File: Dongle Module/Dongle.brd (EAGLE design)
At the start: 45 x 28 mm, 29 parts, among them Q2 2.5A/30V, U1 RFM69HCW, U10 74AHC1G125, U8 ATSAMD21G-A, U9 3.3V, Y1 32.768kHz

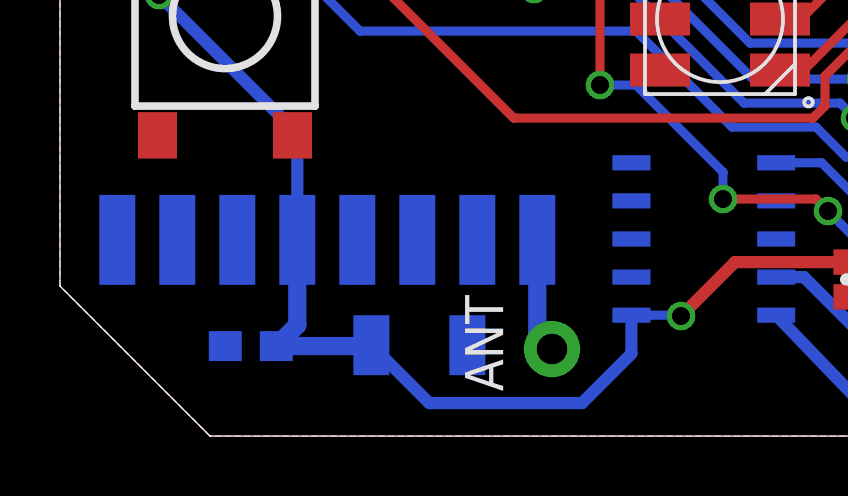
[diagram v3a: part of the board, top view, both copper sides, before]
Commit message: Added the interrupt line from the RFM69 into the Camera Module board. It is connected to GPIO_24
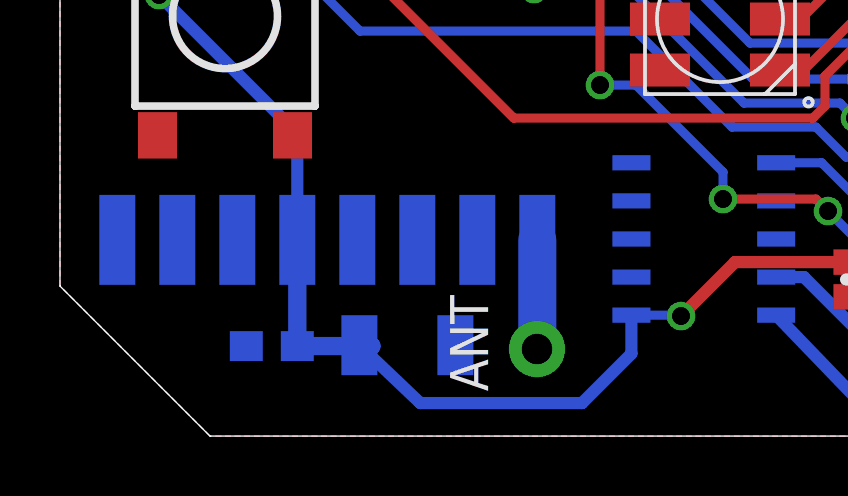
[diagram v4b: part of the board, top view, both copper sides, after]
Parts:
- moved C2 0.70 mm to (7.06, 3.00)
- moved ANT 0.50 mm to (15.9, 2.90)
- moved C1 0.40 mm to (11.6, 3.03)
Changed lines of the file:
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@@
 </autorouter>
 <elements>
-<element name="C1" library="SparkFun-Capacitors" package="1210" value="10uF" x="11.98" y="3.03" smashed="yes" rot="MR180">
-<attribute name="PROD_ID" value="CAP-09824" x="11.98" y="3.03" size="1.778" layer="28" rot="MR180" display="off"/>
-<attribute name="NAME" x="12.32" y="2.77" size="0.4064" layer="26" rot="MR0"/>
+<element name="C1" library="SparkFun-Capacitors" package="1210" value="10uF" x="11.58" y="3.03" smashed="yes" rot="MR180">
+<attribute name="PROD_ID" value="CAP-09824" x="11.58" y="3.03" size="1.778" layer="28" rot="MR180" display="off"/>
+<attribute name="NAME" x="11.92" y="2.77" size="0.4064" layer="26" rot="MR0"/>
 </element>
 <element name="C12" library="SparkFun-Capacitors" package="0402-CAP" value="0.1uF" x="34.25" y="15.33" smashed="yes">
@@
 <attribute name="NAME" x="26.628" y="17.711" size="0.4064" layer="25" font="vector" rot="R90"/>
 </element>
-<element name="C2" library="SparkFun-Capacitors" package="0603-CAP@1" value="0.1uF" x="6.36" y="3" smashed="yes" rot="MR0">
-<attribute name="PROD_ID" value="CAP-00810" x="6.36" y="3" size="1.778" layer="28" rot="MR0" display="off"/>
-<attribute name="NAME" x="6.649" y="4.162" size="0.4064" layer="26" font="vector" rot="MR0"/>
+<element name="C2" library="SparkFun-Capacitors" package="0603-CAP@1" value="0.1uF" x="7.06" y="3" smashed="yes" rot="MR0">
+<attribute name="PROD_ID" value="CAP-00810" x="7.06" y="3" size="1.778" layer="28" rot="MR0" display="off"/>
+<attribute name="NAME" x="7.349" y="4.162" size="0.4064" layer="26" font="vector" rot="MR0"/>
 </element>
 <element name="D7" library="SparkFun-LED" package="LED-0603" value="RED" x="43.34" y="21.8" smashed="yes" rot="R180">
@@
 <attribute name="VALUE" x="25.3" y="18" size="1.27" layer="27" font="vector" rot="R180"/>
 </element>
-<element name="ANT" library="SparkFun-Connectors" package="1X01_NO_SILK" value="" x="16.4" y="2.9" smashed="yes">
-<attribute name="NAME" x="14.7712" y="1.4938" size="1.27" layer="25" rot="R90"/>
-<attribute name="VALUE" x="15.13" y="-0.275" size="1.27" layer="27"/>
+<element name="ANT" library="SparkFun-Connectors" package="1X01_NO_SILK" value="" x="15.9" y="2.9" smashed="yes">
+<attribute name="NAME" x="14.2712" y="1.4938" size="1.27" layer="25" rot="R90"/>
+<attribute name="VALUE" x="14.63" y="-0.275" size="1.27" layer="27"/>
 </element>
 </elements>
@@
 <wire x1="33.64" y1="15.3" x2="33.42" y2="15.08" width="0.3048" layer="1"/>
 <wire x1="33.42" y1="15.08" x2="33.42" y2="13" width="0.3048" layer="1"/>
-<wire x1="7.91" y1="6.54" x2="7.91" y2="3.7" width="0.6096" layer="16"/>
-<wire x1="7.91" y1="3.7" x2="7.21" y2="3" width="0.6096" layer="16"/>
+<wire x1="7.91" y1="6.54" x2="7.91" y2="3" width="0.6096" layer="16"/>
 <wire x1="27.79" y1="17.55" x2="27.82" y2="17.52" width="0.6096" layer="1"/>
 <wire x1="27.82" y1="17.52" x2="30.0799" y2="17.52" width="0.6096" layer="1"/>
@@
 <wire x1="32.5" y1="4.6" x2="28.4" y2="4.6" width="0.3048" layer="16"/>
 <wire x1="33.42" y1="4.5" x2="33.42" y2="7.48" width="0.3048" layer="1"/>
-<wire x1="10.38" y1="3.03" x2="10.38" y2="3" width="0.6096" layer="16"/>
-<wire x1="10.38" y1="3" x2="7.21" y2="3" width="0.6096" layer="16"/>
+<wire x1="9.98" y1="3.03" x2="10.38" y2="3" width="0.6096" layer="16"/>
+<wire x1="10.38" y1="3" x2="7.91" y2="3" width="0.6096" layer="16"/>
 <via x="20.7" y="4" extent="1-16" drill="0.6"/>
 <wire x1="20.7" y1="4" x2="20.7" y2="4.03" width="0.3048" layer="16"/>
@@
 <wire x1="19.047" y1="4.03" x2="19.047" y2="2.747" width="0.4064" layer="16"/>
 <wire x1="19.047" y1="2.747" x2="17.4" y2="1.1" width="0.4064" layer="16"/>
-<wire x1="17.4" y1="1.1" x2="12.31" y2="1.1" width="0.4064" layer="16"/>
-<wire x1="12.31" y1="1.1" x2="10.38" y2="3.03" width="0.4064" layer="16"/>
+<wire x1="17.4" y1="1.1" x2="12.01" y2="1.1" width="0.4064" layer="16"/>
+<wire x1="12.01" y1="1.1" x2="9.98" y2="3.03" width="0.4064" layer="16"/>
 <wire x1="26.23" y1="5.8" x2="22.5" y2="5.8" width="0.4064" layer="1"/>
 <wire x1="22.5" y1="5.8" x2="20.7" y2="4" width="0.4064" layer="1"/>
@@
 <contactref element="U1" pad="9"/>
 <contactref element="ANT" pad="1"/>
-<wire x1="16.4" y1="2.9" x2="15.91" y2="3.39" width="0.6096" layer="16"/>
-<wire x1="15.91" y1="3.39" x2="15.91" y2="6.54" width="0.6096" layer="16"/>
+<wire x1="15.91" y1="6.54" x2="15.91" y2="3.39" width="1.27" layer="16"/>
+<wire x1="15.91" y1="3.39" x2="15.9" y2="2.9" width="1.27" layer="16" curve="90"/>
 </signal>
 <signal name="V_USB">

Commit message: Updated the RFM69 library to be closer to C. millis() is the only function hat needs to be updated now.
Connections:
- new net RF_INT: U1.14, U8.4
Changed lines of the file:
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@@
 <wire x1="24.7" y1="13.9" x2="24" y2="13.9" width="0.3048" layer="1"/>
+</signal>
+<signal name="RF_INT">
+<contactref element="U1" pad="14"/>
+<contactref element="U8" pad="4"/>
+<wire x1="5.91" y1="6.54" x2="36.92" y2="7.5" width="0" layer="19" extent="1-16"/>
 </signal>
 </signals>

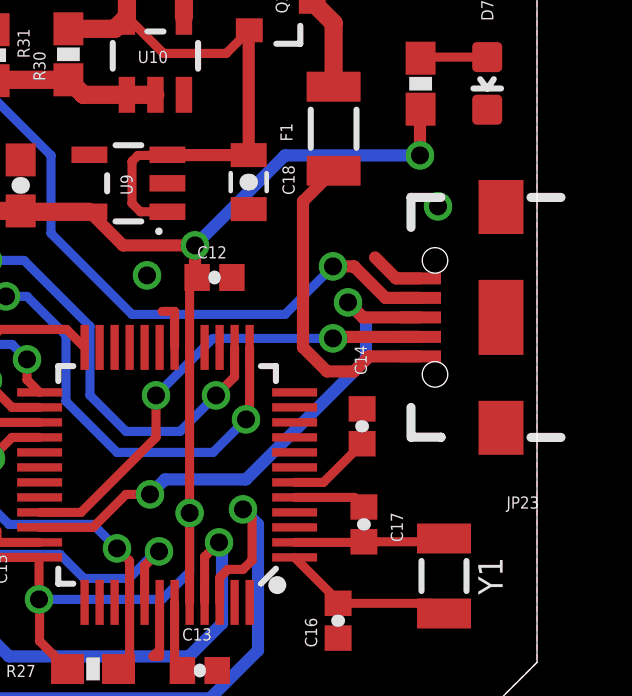
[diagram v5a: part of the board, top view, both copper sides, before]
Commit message: Started the routing of the laser module board Updated the Dongle Module C project to allow for absolute mouse control
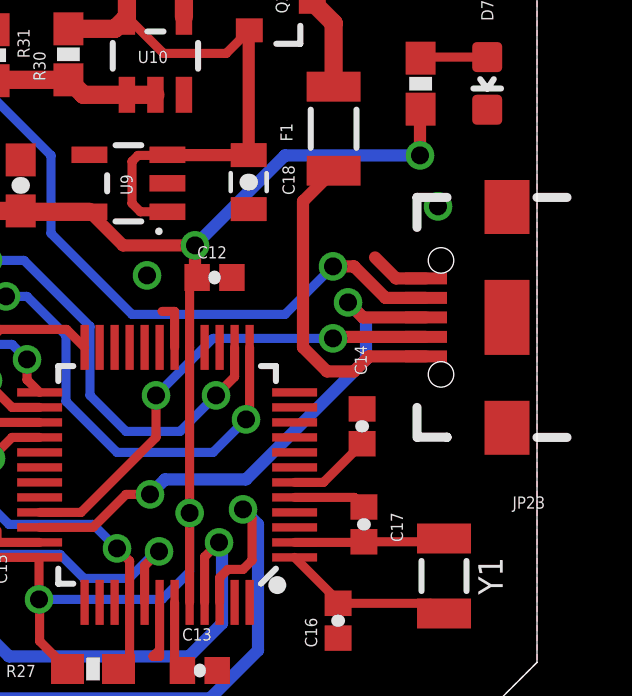
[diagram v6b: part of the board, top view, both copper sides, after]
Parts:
- moved JP23 0.20 mm to (44.0, 14.0)
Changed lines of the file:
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@@
 </element>
 <element name="JP22" library="SparkFun-Connectors" package="SAMTECH_FTSH-105-01" value="CORTEX_DEBUGSMD" x="21.46" y="6.57" smashed="yes" rot="MR90"/>
-<element name="JP23" library="SparkFun-Connectors" package="USB-AB-MICRO-SMD_V03" value="" x="43.8" y="14" rot="R180">
-<attribute name="PROD_ID" value="CONN-11794" x="43.8" y="14" size="1.778" layer="27" rot="R180" display="off"/>
+<element name="JP23" library="SparkFun-Connectors" package="USB-AB-MICRO-SMD_V03" value="" x="44" y="14" rot="R180">
+<attribute name="PROD_ID" value="CONN-11794" x="44" y="14" size="1.778" layer="27" rot="R180" display="off"/>
 </element>
 <element name="Q2" library="SparkFun-DiscreteSemi" package="SOT23-3" value="2.5A/30V" x="36.41" y="24.52" smashed="yes" rot="R270">
@@
 <via x="25.7" y="20.1" extent="1-16" drill="0.6" shape="square"/>
 <via x="41.7" y="17.7" extent="1-16" drill="0.6" shape="square"/>
-<wire x1="41.1" y1="15.3" x2="40.3" y2="15.3" width="0.4064" layer="1"/>
+<wire x1="41.3" y1="15.3" x2="40.3" y2="15.3" width="0.4064" layer="1"/>
 <wire x1="40.3" y1="15.3" x2="39.6" y2="16" width="0.4064" layer="1"/>
 <via x="32" y="15.4" extent="1-16" drill="0.6" shape="square"/>
@@
 <wire x1="38" y1="12.2" x2="38.9" y2="12.2" width="0.4064" layer="1"/>
 <wire x1="38.9" y1="12.2" x2="39.4" y2="12.7" width="0.4064" layer="1"/>
-<wire x1="39.4" y1="12.7" x2="41.1" y2="12.7" width="0.4064" layer="1"/>
+<wire x1="39.4" y1="12.7" x2="41.3" y2="12.7" width="0.4064" layer="1"/>
 </signal>
 <signal name="VDDCORE">
@@
 <via x="38.7" y="14.5" extent="1-16" drill="0.6"/>
 <wire x1="39.3" y1="13.9" x2="38.7" y2="14.5" width="0.4064" layer="16"/>
-<wire x1="41.1" y1="14" x2="39.2" y2="14" width="0.4064" layer="1"/>
+<wire x1="41.3" y1="14" x2="39.2" y2="14" width="0.4064" layer="1"/>
 <wire x1="39.2" y1="14" x2="38.7" y2="14.5" width="0.4064" layer="1"/>
 </signal>
@@
 <via x="38.2" y="13.3" extent="1-16" drill="0.6"/>
 <wire x1="38.2" y1="13.3" x2="38.25" y2="13.35" width="0.4064" layer="1"/>
-<wire x1="38.25" y1="13.35" x2="41.1" y2="13.35" width="0.4064" layer="1"/>
+<wire x1="38.25" y1="13.35" x2="41.3" y2="13.35" width="0.4064" layer="1"/>
 <wire x1="34.2" y1="13.3" x2="38.2" y2="13.3" width="0.3048" layer="16"/>
 <wire x1="29.8" y1="7.5" x2="32.3" y2="10" width="0.3048" layer="1"/>
@@
 <wire x1="31.33" y1="21.4199" x2="32.28" y2="21.4199" width="0.6096" layer="1"/>
 <via x="38.2" y="15.7" extent="1-16" drill="0.6"/>
-<wire x1="41.1" y1="14.65" x2="39.95" y2="14.65" width="0.4064" layer="1"/>
+<wire x1="41.3" y1="14.65" x2="39.95" y2="14.65" width="0.4064" layer="1"/>
 <wire x1="39.95" y1="14.65" x2="38.9" y2="15.7" width="0.4064" layer="1"/>
 <wire x1="38.9" y1="15.7" x2="38.2" y2="15.7" width="0.4064" layer="1"/>

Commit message: Added text to the Dongle Module board
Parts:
- added U$2: (no value), MAAV_BlockM:BLOCK-M-5MM
- added U$3: (no value), MAAV_BlockM:BLOCK-M-5MM-MASK
- moved C16 2.12 mm to (40.5, 3.59)
- moved C17 1.20 mm to (40.4, 7.10)
- moved Y1 0.70 mm to (42.6, 5.38)
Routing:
- net RF_INT: track 0.00 -> 46.0 mm, vias 0 -> 3
- net N$10: track 5.78 -> 6.45 mm
- net N$13: track 5.09 -> 5.73 mm
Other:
- board text added: "AIZER"
- board text added: "Designed By: Matt Sauvé"
- board text added: "Dongle Module"
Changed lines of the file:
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@@
 <wire x1="42.5" y1="28" x2="5" y2="28" width="0" layer="20"/>
 <wire x1="5" y1="28" x2="0" y2="23" width="0" layer="20"/>
+<text x="32.6" y="23.4" size="2.1844" layer="22" ratio="12" rot="MR0">AIZER</text>
+<text x="37.8" y="21.9" size="0.8128" layer="22" ratio="12" rot="MR0">Dongle Module</text>
+<text x="41.2" y="0.9" size="0.8128" layer="22" ratio="10" rot="MR0">Designed By: Matt Sauvé</text>
 </plain>
 <attributes>
@@
 <attribute name="NAME" x="26.9285" y="6.109" size="0.4064" layer="25" rot="R270"/>
 </element>
-<element name="C16" library="samd21-temp" package="0402-CAP" value="15pF" x="38.37" y="3.89" smashed="yes" rot="R90">
-<attribute name="PROD_ID" value="CAP-13063" x="38.37" y="3.89" size="1.778" layer="27" rot="R90" display="off"/>
-<attribute name="NAME" x="37.6715" y="3.001" size="0.4064" layer="25" rot="R90"/>
-</element>
-<element name="C17" library="samd21-temp" package="0402-CAP" value="15pF" x="39.23" y="7.1" smashed="yes" rot="R90">
-<attribute name="PROD_ID" value="CAP-13063" x="39.23" y="7.1" size="1.778" layer="27" rot="R90" display="off"/>
-<attribute name="NAME" x="40.5315" y="6.511" size="0.4064" layer="25" rot="R90"/>
+<element name="C16" library="samd21-temp" package="0402-CAP" value="15pF" x="40.47" y="3.59" smashed="yes" rot="R90">
+<attribute name="PROD_ID" value="CAP-13063" x="40.47" y="3.59" size="1.778" layer="27" rot="R90" display="off"/>
+<attribute name="NAME" x="39.7715" y="2.701" size="0.4064" layer="25" rot="R90"/>
+</element>
+<element name="C17" library="samd21-temp" package="0402-CAP" value="15pF" x="40.43" y="7.1" smashed="yes" rot="R90">
+<attribute name="PROD_ID" value="CAP-13063" x="40.43" y="7.1" size="1.778" layer="27" rot="R90" display="off"/>
+<attribute name="NAME" x="41.7315" y="6.511" size="0.4064" layer="25" rot="R90"/>
 </element>
 <element name="C18" library="SparkFun-Capacitors" package="0805-CAP" value="1.0uF" x="35.39" y="18.51" smashed="yes" rot="R270">
@@
 <attribute name="NAME" x="31.521" y="18.081" size="0.4064" layer="25" rot="R90"/>
 </element>
-<element name="Y1" library="samd21-temp" package="CRYSTAL-SMD-3.2X1.5MM" value="32.768kHz" x="41.9" y="5.38" smashed="yes" rot="R270">
-<attribute name="PROD_ID" value="XTAL-13062" x="41.9" y="5.38" size="1.778" layer="27" rot="R270" display="off"/>
-<attribute name="NAME" x="43.043" y="5.38" size="0.8128" layer="25" rot="R270" align="bottom-center"/>
+<element name="Y1" library="samd21-temp" package="CRYSTAL-SMD-3.2X1.5MM" value="32.768kHz" x="42.6" y="5.38" smashed="yes" rot="R270">
+<attribute name="PROD_ID" value="XTAL-13062" x="42.6" y="5.38" size="1.778" layer="27" rot="R270" display="off"/>
+<attribute name="NAME" x="42.82" y="2.443" size="0.8128" layer="25" align="bottom-center"/>
 </element>
 <element name="S1" library="SparkFun-Electromechanical" package="TACTILE_SWITCH_TALL" value="SWITCH-MOMENTARY-2SMD-4" x="5.5" y="14" smashed="yes" rot="R90">
@@
 <attribute name="PROD_ID" value="RES-00818" x="6.9" y="20.5" size="1.778" layer="27" display="off"/>
 </element>
-<element name="U$1" library="SAUVE" package="APA102" value="APA102" x="22" y="13.9" smashed="yes" rot="R180">
-<attribute name="VALUE" x="25.3" y="18" size="1.27" layer="27" font="vector" rot="R180"/>
-</element>
+<element name="U$1" library="SAUVE" package="APA102" value="APA102" x="22" y="13.9" smashed="yes" rot="R180"/>
 <element name="ANT" library="SparkFun-Connectors" package="1X01_NO_SILK" value="" x="15.9" y="2.9" smashed="yes">
-<attribute name="NAME" x="14.2712" y="1.4938" size="1.27" layer="25" rot="R90"/>
+<attribute name="NAME" x="14.7062" y="3.4712" size="1.27" layer="25" rot="R180"/>
 <attribute name="VALUE" x="14.63" y="-0.275" size="1.27" layer="27"/>
 </element>
+<element name="U$2" library="MAAV_BlockM" package="BLOCK-M-5MM" value="" x="35.6" y="25.1" rot="MR0"/>
+<element name="U$3" library="MAAV_BlockM" package="BLOCK-M-5MM-MASK" value="" x="13.4" y="23.6"/>
 </elements>
 <signals>
@@
 <vertex x="45" y="2.5"/>
 </polygon>
-<wire x1="36.92" y1="8" x2="38.91" y2="8" width="0.3048" layer="1"/>
-<wire x1="38.91" y1="8" x2="39.23" y2="7.68" width="0.3048" layer="1"/>
 <wire x1="32.42" y1="4.5" x2="32.42" y2="2.7" width="0.3048" layer="1"/>
 <wire x1="32.42" y1="2.7" x2="32.2" y2="2.7" width="0.3048" layer="1"/>
@@
 <wire x1="40.3" y1="15.3" x2="39.6" y2="16" width="0.4064" layer="1"/>
 <via x="32" y="15.4" extent="1-16" drill="0.6" shape="square"/>
+<wire x1="36.92" y1="8" x2="38.2" y2="8" width="0.3048" layer="1"/>
+<wire x1="38.2" y1="8" x2="38.7" y2="8.5" width="0.3048" layer="1"/>
 </signal>
 <signal name="3.3V">
@@
 <contactref element="Y1" pad="P$2"/>
 <contactref element="C16" pad="2"/>
-<wire x1="38.37" y1="4.47" x2="38.37" y2="4.55" width="0.3048" layer="1"/>
-<wire x1="38.37" y1="4.55" x2="36.92" y2="6" width="0.3048" layer="1"/>
-<wire x1="41.9" y1="4.13" x2="41.46" y2="4.47" width="0.3048" layer="1"/>
-<wire x1="41.46" y1="4.47" x2="38.37" y2="4.47" width="0.3048" layer="1"/>
+<wire x1="42.6" y1="4.13" x2="42.56" y2="4.17" width="0.3048" layer="1"/>
+<wire x1="42.56" y1="4.17" x2="40.47" y2="4.17" width="0.3048" layer="1"/>
+<wire x1="40.47" y1="4.17" x2="38.64" y2="6" width="0.3048" layer="1"/>
+<wire x1="38.64" y1="6" x2="36.92" y2="6" width="0.3048" layer="1"/>
 </signal>
 <signal name="N$13">
@@
 <contactref element="Y1" pad="P$1"/>
 <contactref element="U8" pad="2"/>
-<wire x1="39.23" y1="6.52" x2="39.21" y2="6.5" width="0.3048" layer="1"/>
-<wire x1="39.21" y1="6.5" x2="36.92" y2="6.5" width="0.3048" layer="1"/>
-<wire x1="41.9" y1="6.63" x2="41.89" y2="6.52" width="0.3048" layer="1"/>
-<wire x1="41.89" y1="6.52" x2="39.23" y2="6.52" width="0.3048" layer="1"/>
+<wire x1="42.6" y1="6.63" x2="40.54" y2="6.63" width="0.3048" layer="1"/>
+<wire x1="40.54" y1="6.63" x2="40.43" y2="6.52" width="0.3048" layer="1"/>
+<wire x1="40.43" y1="6.52" x2="40.41" y2="6.5" width="0.3048" layer="1"/>
+<wire x1="40.41" y1="6.5" x2="36.92" y2="6.5" width="0.3048" layer="1"/>
 </signal>
 <signal name="!RESET">
@@
 <contactref element="U1" pad="14"/>
 <contactref element="U8" pad="4"/>
-<wire x1="5.91" y1="6.54" x2="36.92" y2="7.5" width="0" layer="19" extent="1-16"/>
+<via x="38.9" y="7.4" extent="1-16" drill="0.6"/>
+<via x="5.9" y="9.1" extent="1-16" drill="0.6"/>
+<wire x1="38.9" y1="7.4" x2="38.8" y2="7.5" width="0.3048" layer="1"/>
+<wire x1="38.8" y1="7.5" x2="36.92" y2="7.5" width="0.3048" layer="1"/>
+<wire x1="5.91" y1="6.54" x2="5.9" y2="6.55" width="0.3048" layer="16"/>
+<wire x1="5.9" y1="6.55" x2="5.9" y2="9.1" width="0.3048" layer="16"/>
+<wire x1="5.9" y1="9.1" x2="9.6" y2="5.4" width="0.3048" layer="1"/>
+<wire x1="9.6" y1="5.4" x2="16.7" y2="5.4" width="0.3048" layer="1"/>
+<wire x1="16.7" y1="5.4" x2="21.3" y2="0.8" width="0.3048" layer="1"/>
+<wire x1="21.3" y1="0.8" x2="36.1" y2="0.8" width="0.3048" layer="1"/>
+<wire x1="36.1" y1="0.8" x2="37.8" y2="2.5" width="0.3048" layer="1"/>
+<via x="37.8" y="2.5" extent="1-16" drill="0.6"/>
+<wire x1="37.8" y1="2.5" x2="38.9" y2="3.6" width="0.3048" layer="16"/>
+<wire x1="38.9" y1="3.6" x2="38.9" y2="7.4" width="0.3048" layer="16"/>
 </signal>
 </signals>

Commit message: Finalized all PCBs
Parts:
- removed U$3: (no value), MAAV_BlockM:BLOCK-M-5MM-MASK
- added U$4: (no value), MAAV_BlockM:BLOCK-M-10MM-MASK
- C12, C13, C14, C15: device SparkFun-Capacitors:0402-CAP -> SparkFun-Capacitors:0603-CAP
- C16, C17: device samd21-temp:0402-CAP -> SparkFun-Capacitors:0603-CAP
- C2: device SparkFun-Capacitors:0603-CAP@1 -> SparkFun-Capacitors:0603-CAP
- D7: value RED -> GREEN
- moved C13 0.45 mm to (34.2, 2.43)
- moved C17 0.41 mm to (40.8, 7.20)
- moved C15 0.40 mm to (26.2, 4.82)
- moved Y1 0.40 mm to (43.0, 5.38)
- moved C12 0.36 mm to (34.5, 15.0)
- moved C16 0.36 mm to (40.3, 3.29)
- moved JP23 0.15 mm to (43.9, 14.0)
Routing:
- net USB_HOST_EN: track 38.0 -> 37.2 mm
- net 3.3V: track 90.6 -> 91.4 mm
- net RF_SS: track 24.7 -> 25.3 mm
